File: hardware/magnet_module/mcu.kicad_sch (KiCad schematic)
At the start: 26 parts, among them J9 STLINK-V3-MINIE, SW1 SW_DIP_x02, SW2 CK_PTS526_SK15_Switch, SW3 CK_PTS526_SK15_Switch, U3 W25Q16JVSSIQ, U8 STM32G474RETx

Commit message: Make schematic changes for the following v1.1 changes: * Add directional & latching connector to GPIO0 & GPIO1 * Add CAN IN / CAN OUT directionality * Add pulldown to BOOT pin and pullup to nRST * Correct servo orientation
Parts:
- added R25, R26: 10k, Resistor_SMD:R_0603_1608Metric, symbol Device:R
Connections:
- net 3V3: now also SW3.1, SW3.2, R26.1
- net BOOT: now also R25.1
- net GND: now also R25.2; no longer SW3.1, SW3.2
- net ~{MCU_RST}: now also R26.2
- net GPIO0 renamed CONT0
- net GPIO1 renamed CONT1
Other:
- moved on the sheet: C19, J9, SW2, SW3, TP10, TP11

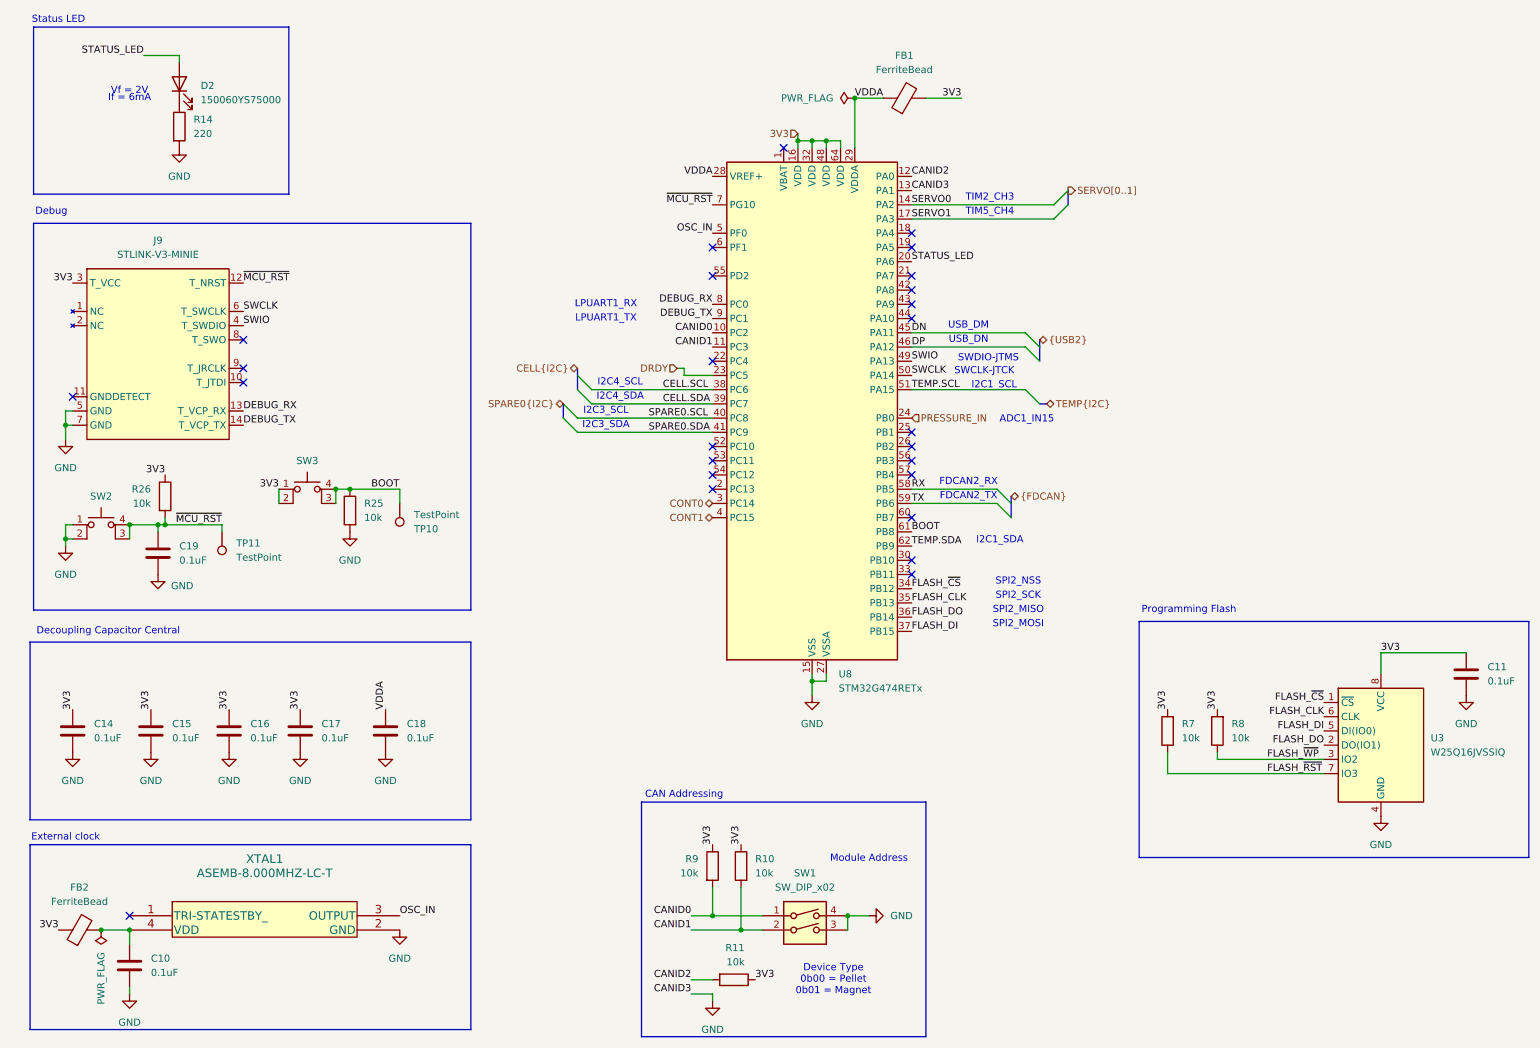
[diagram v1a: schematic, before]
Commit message: add test points to schematic, generate step file including ultrasonic mic
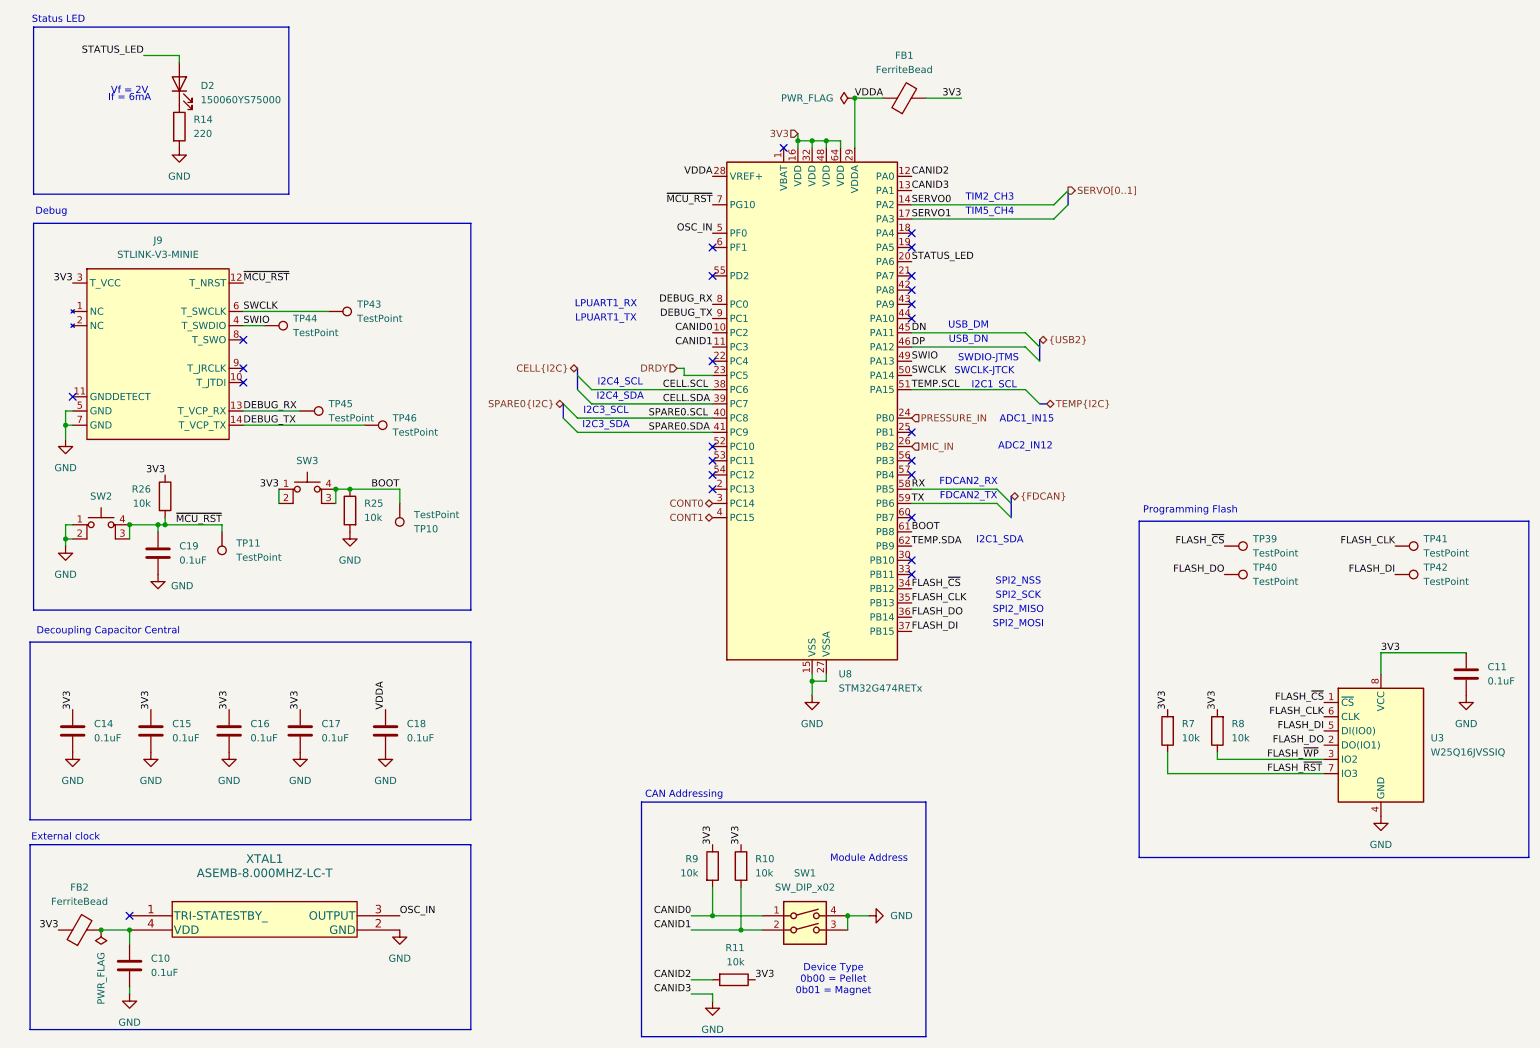
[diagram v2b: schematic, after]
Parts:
- added TP39, TP40, TP41, TP42, TP43, TP44, TP45, TP46: TestPoint, TestPoint:TestPoint_Pad_1.0x1.0mm, symbol Connector:TestPoint
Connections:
- net DEBUG_RX: now also TP45.1
- net DEBUG_TX: now also TP46.1
- net FLASH_CLK: now also TP41.1
- net FLASH_DI: now also TP42.1
- net FLASH_DO: now also TP40.1
- net FLASH_~{CS}: now also TP39.1
- net SWCLK: now also TP43.1
- net SWIO: now also TP44.1
- net MIC_IN: now reaches U8.26 (PB2)
- no-connect marks 26 -> 25
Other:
- note added: "ADC2_IN12"

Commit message: Lay out requested Alogus changes and ensure every part has a MPN & LCSC PN
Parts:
- J9: now left out of the parts list
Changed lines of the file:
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@@
 		(at 36.83 67.31 0)
 		(unit 1)
-		(exclude_from_sim no)
-		(in_bom yes)
+		(exclude_from_sim yes)
+		(in_bom no)
 		(on_board yes)
 		(dnp no)

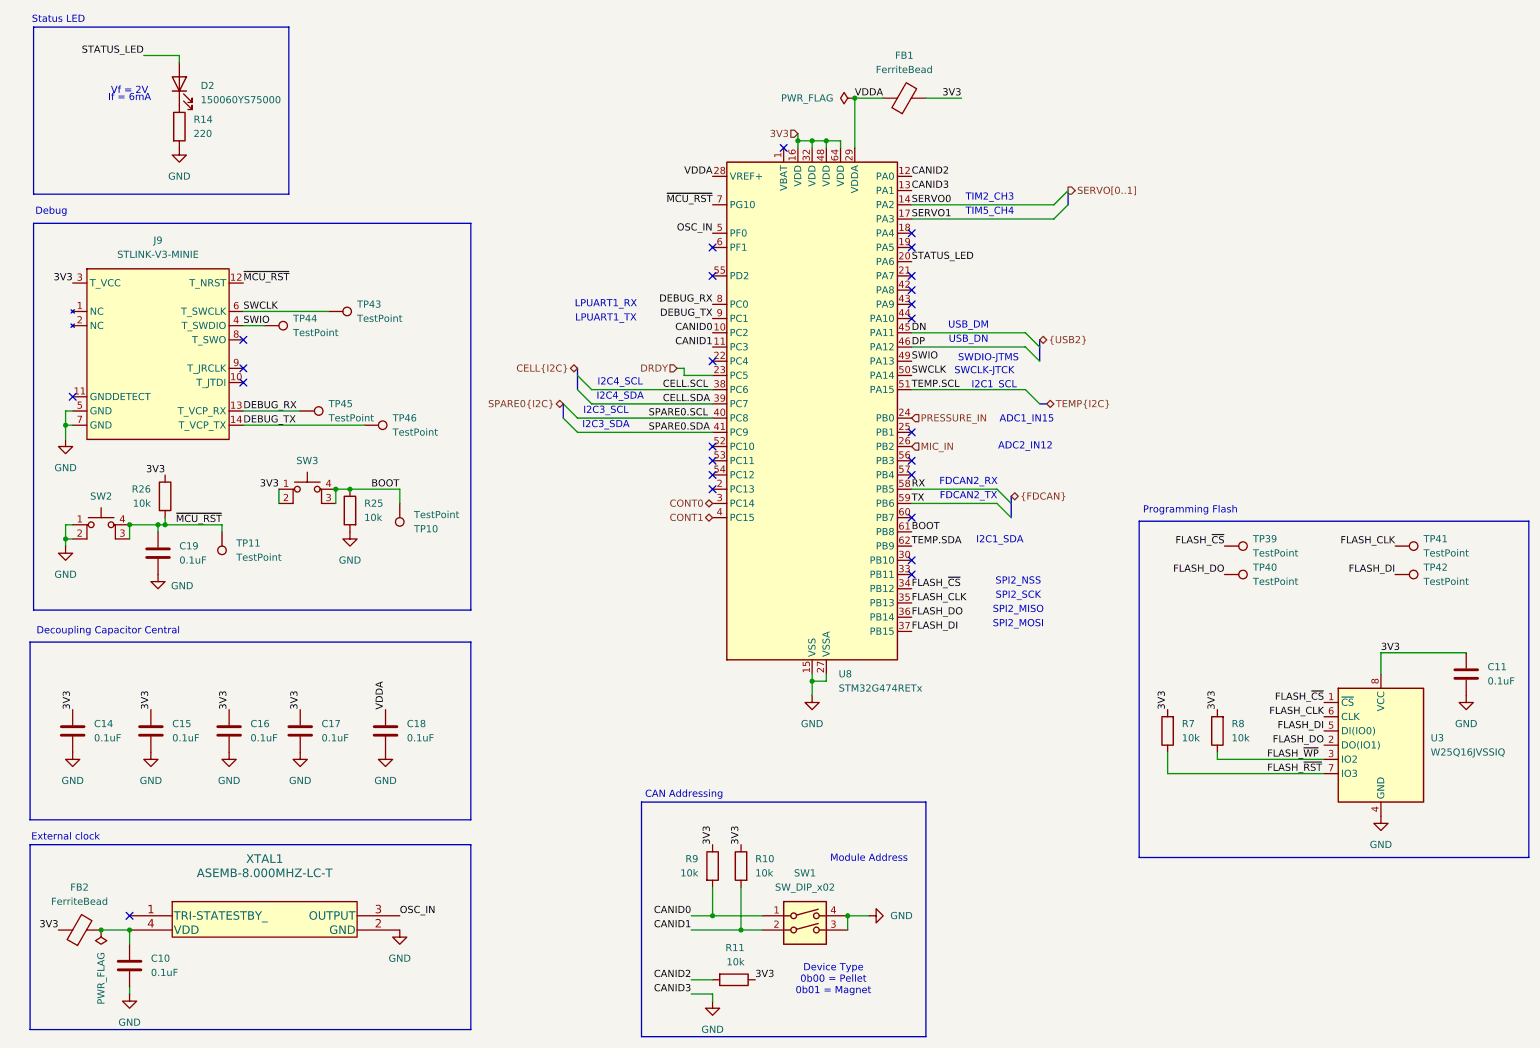
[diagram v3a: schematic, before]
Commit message: Add ultrasonic microphone
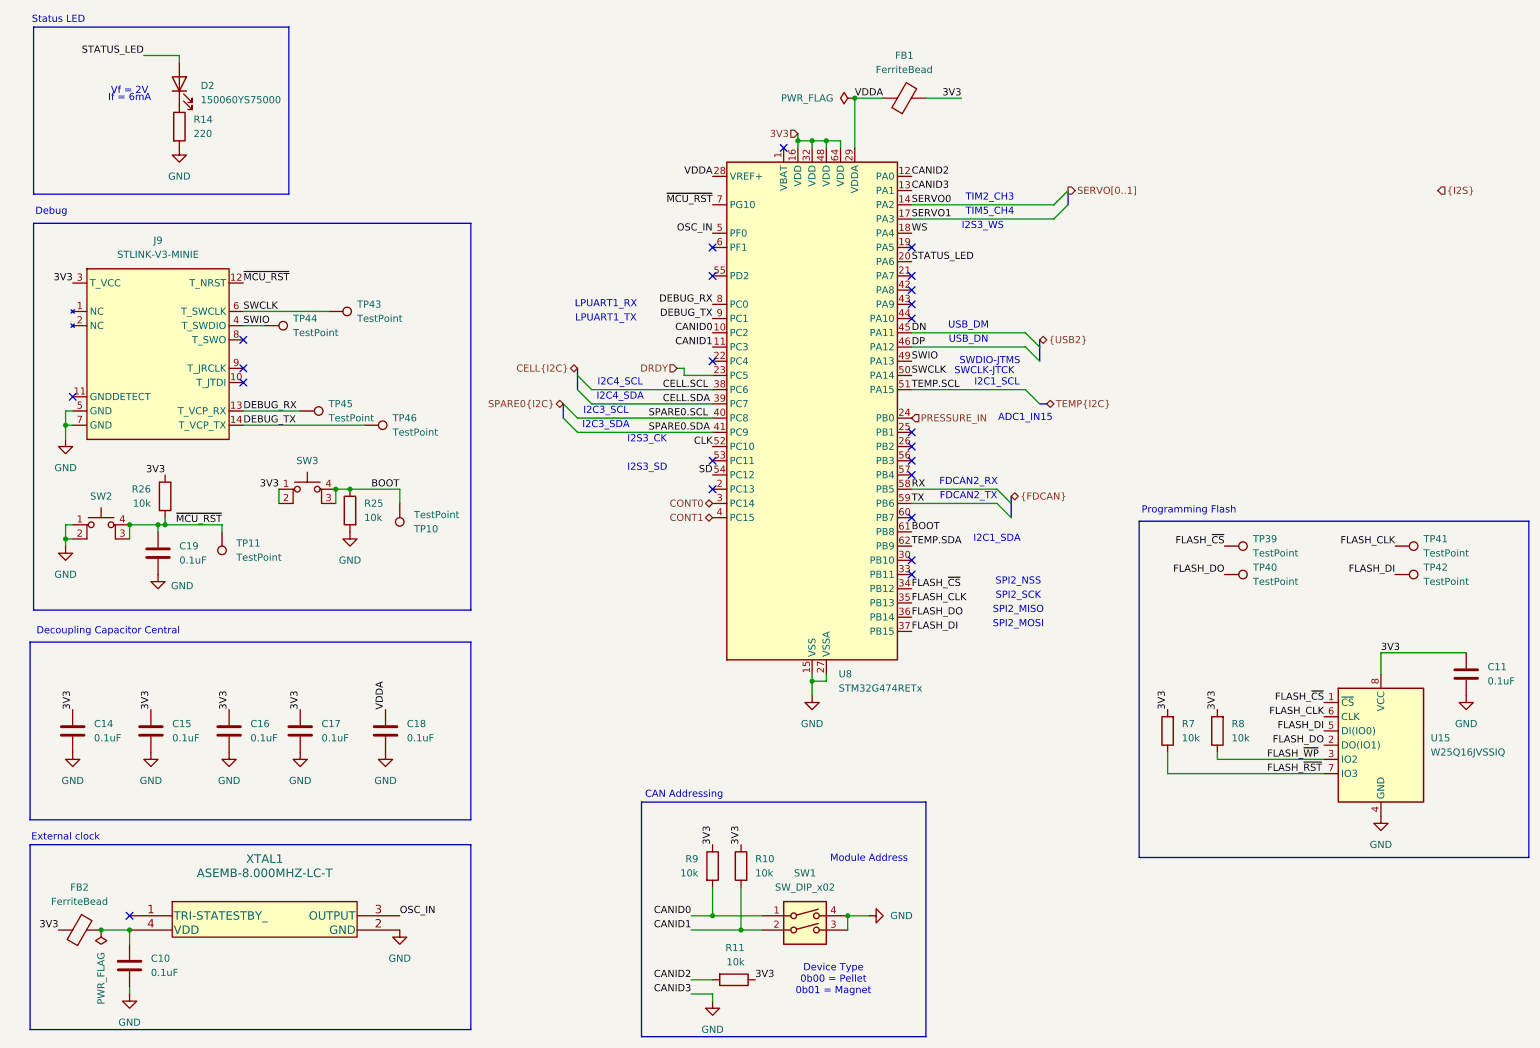
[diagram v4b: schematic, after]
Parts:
- renumbered U3 to U15
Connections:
- net WS: now reaches U8.18 (PA4)
- net CLK: now reaches U8.52 (PC10)
- net SD: now reaches U8.54 (PC12)
- net MIC_IN: no longer names the net of U8.26 (PB2)
- no-connect marks 25 -> 23
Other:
- note added: "I2S3_CK"
- note added: "I2S3_SD"
- note added: "I2S3_WS"
- note removed: "ADC2_IN12"
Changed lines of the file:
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@@
-	)
-	(no_connect
-		(at 171.45 53.34)
 	)
 	(no_connect
@@
 	)
 	(no_connect
+		(at 171.45 91.44)
+	)
+	(no_connect
 		(at 21.59 82.55)
 	)
@@
 	)
 	(no_connect
-		(at 135.89 96.52)
-	)
-	(no_connect
 		(at 135.89 76.2)
 	)
@@
 	(no_connect
 		(at 171.45 55.88)
-	)
-	(no_connect
-		(at 135.89 91.44)
 	)
 	(bus_entry
@@
 		)
 	)
+	(text "I2S3_CK"
+		(exclude_from_sim no)
+		(at 120.65 90.17 0)
+		(effects
+			(font
+				(size 1.27 1.27)
+			)
+			(justify left)
+		)
+	)
 	(text "SWCLK-JTCK"
 		(exclude_from_sim no)
@@
 	(text "I2C1_SDA"
 		(exclude_from_sim no)
-		(at 187.198 108.204 0)
+		(at 186.69 107.95 0)
 		(effects
 			(font
@@
 	(text "ADC1_IN15"
 		(exclude_from_sim no)
-		(at 192.024 86.614 0)
+		(at 191.77 86.36 0)
 		(effects
 			(font
@@
 	(text "I2C1_SCL"
 		(exclude_from_sim no)
-		(at 186.182 80.518 0)
+		(at 186.69 80.01 0)
 		(effects
 			(font
@@
 		)
 	)
-	(text "ADC2_IN12"
-		(exclude_from_sim no)
-		(at 191.77 91.44 0)
-		(effects
-			(font
-				(size 1.27 1.27)
-			)
-		)
-	)
 	(text "Module Address"
 		(exclude_from_sim no)
@@
 	(text "Programming Flash"
 		(exclude_from_sim no)
-		(at 221.234 102.87 0)
+		(at 220.98 102.87 0)
 		(effects
 			(font
@@
 		)
 	)
+	(text "I2S3_WS"
+		(exclude_from_sim no)
+		(at 184.15 52.07 0)
+		(effects
+			(font
+				(size 1.27 1.27)
+			)
+		)
+	)
+	(text "I2S3_SD"
+		(exclude_from_sim no)
+		(at 120.65 95.25 0)
+		(effects
+			(font
+				(size 1.27 1.27)
+			)
+			(justify left)
+		)
+	)
 	(text "SPI2_SCK"
 		(exclude_from_sim no)
@@
 	(text "SWDIO-JTMS"
 		(exclude_from_sim no)
-		(at 185.166 75.692 0)
+		(at 185.42 76.2 0)
 		(effects
 			(font
@@
 		)
 	)
+	(label "WS"
+		(at 171.45 53.34 0)
+		(effects
+			(font
+				(size 1.27 1.27)
+			)
+			(justify left bottom)
+		)
+	)
 	(label "3V3"
 		(at 62.23 138.43 90)
@@
 		)
 	)
+	(label "SD"
+		(at 135.89 96.52 180)
+		(fields_autoplaced yes)
+		(effects
+			(font
+				(size 1.27 1.27)
+			)
+			(justify right bottom)
+		)
+	)
 	(label "3V3"
 		(at 217.17 138.43 90)
@@
 			)
 			(justify left bottom)
+		)
+	)
+	(label "CLK"
+		(at 135.89 91.44 180)
+		(fields_autoplaced yes)
+		(effects
+			(font
+				(size 1.27 1.27)
+			)
+			(justify right bottom)
 		)
 	)
@@
 		)
 	)
+	(hierarchical_label "{I2S}"
+		(shape input)
+		(at 265.43 45.72 0)
+		(fields_autoplaced yes)
+		(effects
+			(font
+				(size 1.27 1.27)
+			)
+			(justify left)
+		)
+	)
 	(hierarchical_label "CONT0"
 		(shape bidirectional)
@@
 		(shape bidirectional)
 		(at 195.58 83.82 0)
-		(fields_autoplaced yes)
-		(effects
-			(font
-				(size 1.27 1.27)
-			)
-			(justify left)
-		)
-	)
-	(hierarchical_label "MIC_IN"
-		(shape input)
-		(at 171.45 91.44 0)
 		(fields_autoplaced yes)
 		(effects
@@
 		(dnp no)
 		(fields_autoplaced yes)
-		(property "Reference" "U3"
+		(property "Reference" "U15"
 			(at 264.16 143.5099 0)
 			(effects
@@
 		(pin "1"
 		)
-	)
+		(instances
+			(project "magnet"
+				(path "/aa5044b8-67cd-4b5a-a593-0df9431eb095/286cc8bf-34fd-48cd-9d6c-58653d0694aa"
+					(reference "U15")
+					(unit 1)
+				)
+			)
+		)
+	)
